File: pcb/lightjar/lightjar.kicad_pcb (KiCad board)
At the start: 2 copper layers, 21 parts, among them J1 Power/Comms, J2 Button, J3 Photoresistor, J4 Potentiometer, Q1 MMBTA42, U1 AMS1117-5.0, U2 Pico

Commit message: Layout and schematic updates
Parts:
- removed C5: 0.1 uF, Capacitor_SMD:C_0805_2012Metric_Pad1.18x1.45mm_HandSolder
- D1, D2: footprint Diode_SMD:D_1206_3216Metric_Pad1.42x1.75mm_HandSolder -> Diode_SMD:D_SOD-123
- R6: value 125 -> 220
- moved D2 87.1 mm to (150.0, 126.0), turned to -90 degrees
- moved J3 27.3 mm to (169.8, 73.8), turned to 90 degrees
- moved R4 24.2 mm to (163.5, 74.0), turned to 90 degrees
- moved R2 17.8 mm to (165.0, 70.7), turned to -90 degrees
- moved C4 15.0 mm to (163.0, 68.0)
- moved J1 14.5 mm to (169.8, 65.0)
- moved C1 13.3 mm to (161.9, 45.0), turned to -90 degrees
- moved D1 11.2 mm to (161.9, 38.8), turned to 90 degrees
- moved R6 10.7 mm to (162.0, 53.5), turned to 0 degrees
- moved C2 10.0 mm to (155.0, 46.5), turned to 180 degrees
- moved F1 9.85 mm to (168.5, 43.5), turned to 0 degrees
- moved Q1 8.87 mm to (158.3, 52.5)
- moved R5 6.91 mm to (162.0, 51.5)
- moved C3 4.11 mm to (162.7, 61.5)
- moved U1 3.65 mm to (156.7, 40.4), turned to 90 degrees
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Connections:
- C3 pad 1: Brightness -> Brightness Pin
- C4 pad 1: Photoresistor -> Photoresistor Pin
- Q1 pad 2: WS2315 Output -> WS2815 Output
- Q1 pad 3: +3.3V -> +5V
- R2 pad 1: Photoresistor -> Photoresistor Pin
- R3 pad 1: Brightness -> Brightness Pin
- R5 pad 1: WS2315 Output -> WS2815 Output
- U2 pad 20: unconnected-(U2-GPIO15-Pad20) -> WS2815 Pin
- U2 pad 27: WS2815 Pin -> unconnected-(U2-GPIO21-Pad27)
- U2 pad 31: unconnected-(U2-GPIO26_ADC0-Pad31) -> Photoresistor Pin
- U2 pad 32: Photoresistor -> Brightness Pin
- U2 pad 34: Brightness -> unconnected-(U2-GPIO28_ADC2-Pad34)
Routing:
- net +5V: track 14.3 -> 155.0 mm, vias 0 -> 2
- net Brightness Pin: track 0.00 -> 62.2 mm
- net Photoresistor Pin: track 0.00 -> 60.2 mm
- net +3.3V: track 111.9 -> 63.1 mm
- net Button Sig: track 6.54 -> 35.9 mm
- net +12V: track 0.00 -> 23.8 mm
- net WS2815 Pin: track 52.8 -> 33.5 mm
- net Net-(D2-K): track 16.6 -> 4.23 mm
- net WS2815 Output: track 0.00 -> 11.8 mm
- net +12VA: track 0.00 -> 4.13 mm
- net Photoresistor: track 2.04 -> 0.00 mm
- net Brightness: track 1.95 -> 0.00 mm
- net Photoresistor Sig: track 6.72 -> 7.48 mm
- net GND: vias 0 -> 31
- added copper zone on F.Cu, net +5V
- added copper zone on B.Cu, net GND
- added copper zone on F.Cu, net GND
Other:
- board outline added: 30 x 97 mm
- board text added: "+"
- board text added: "-"
- board text added: "12IN"
- board text added: "12OUT"
- board text added: "Button"
- board text added: "GND"
- board text added: "Photoresistor"
- board text added: "Potentiometer"
- board text added: "Power/WS2815"
- board text added: "SIG"
- board text added: "Sig"

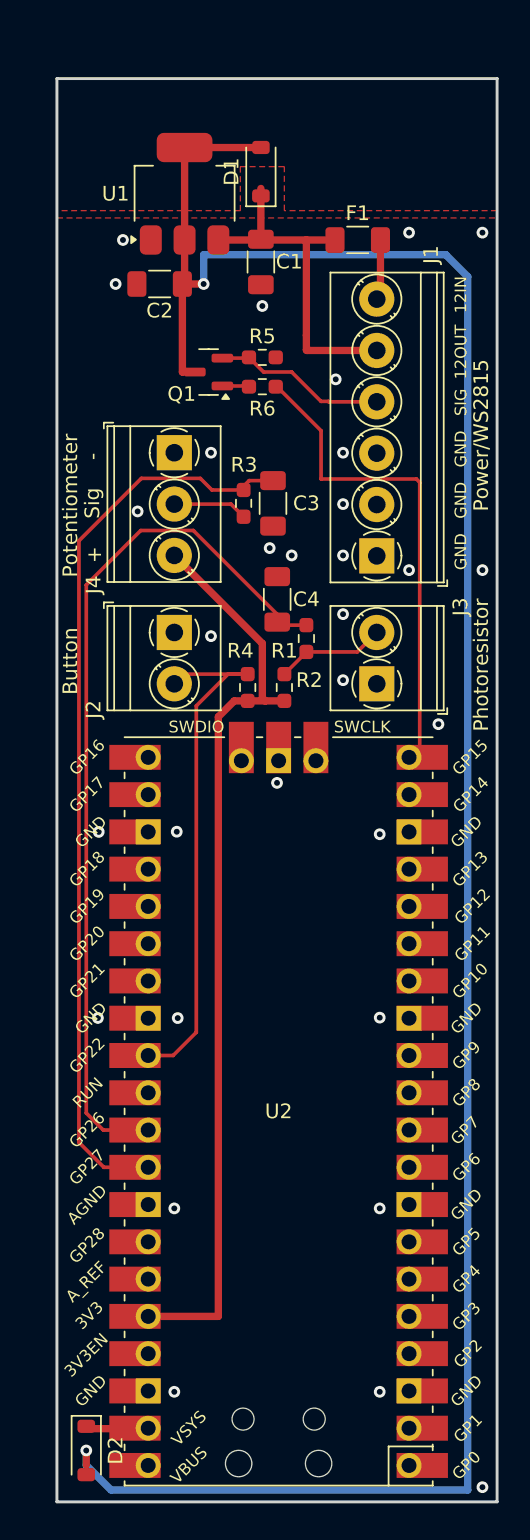
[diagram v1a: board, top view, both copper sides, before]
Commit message: Update to FET driver design
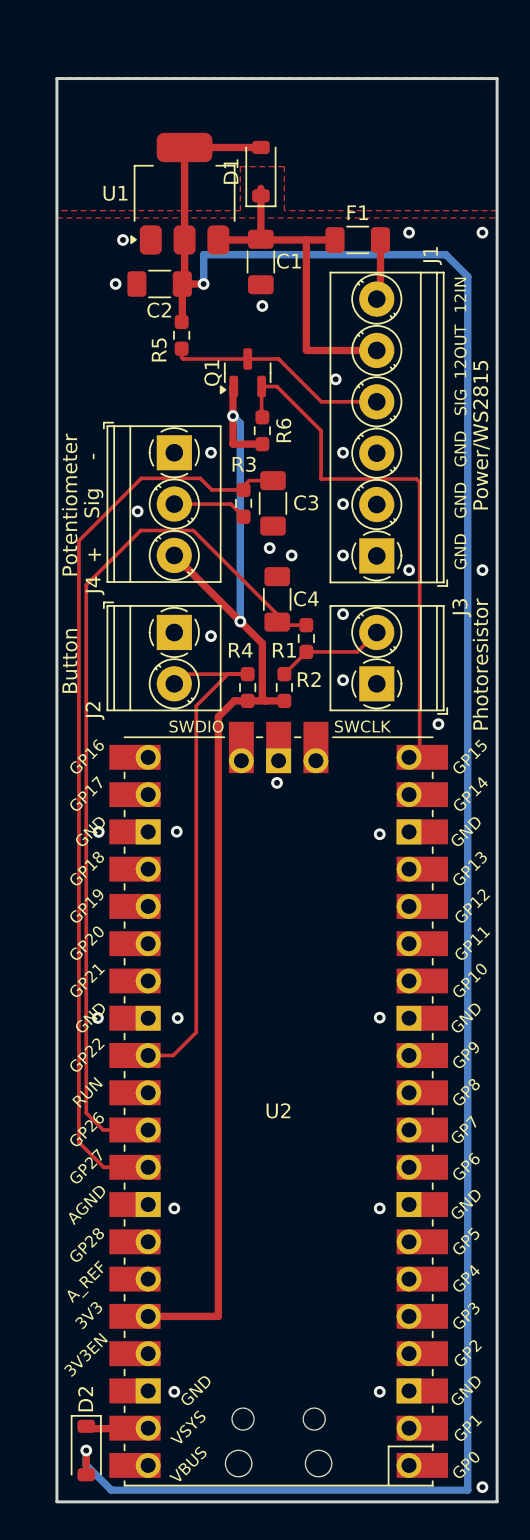
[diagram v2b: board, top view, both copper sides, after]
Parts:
- Q1: value MMBTA42 -> IRLML2803PbF
- R5: value 20k -> 10k
- R6: value 220 -> 10k
- moved R5 5.70 mm to (156.5, 50.0), turned to -90 degrees
- moved R6 3.00 mm to (162.0, 56.5), turned to 90 degrees
- moved Q1 2.66 mm to (161.0, 52.5), turned to 90 degrees
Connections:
- Q1 pad 1: Net-(Q1-B) -> +3.3V
- Q1 pad 2: WS2815 Output -> WS2815 Pin
- Q1 pad 3: +5V -> WS2815 Output
- R5 pad 1: WS2815 Output -> +5V
- R5 pad 2: GND -> WS2815 Output
- R6 pad 1: Net-(Q1-B) -> +3.3V
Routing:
- net +3.3V: track 63.1 -> 82.8 mm, vias 0 -> 2
- net +5V: track 155.0 -> 150.8 mm
- net WS2815 Output: track 11.8 -> 15.1 mm
- net WS2815 Pin: track 33.5 -> 36.2 mm
- net Net-(Q1-B): track 1.90 -> 0.00 mm
